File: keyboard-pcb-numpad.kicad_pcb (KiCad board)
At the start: 2 copper layers, 100 x 99 mm, 37 parts, among them SW1 SW_Push, U1 ProMicro

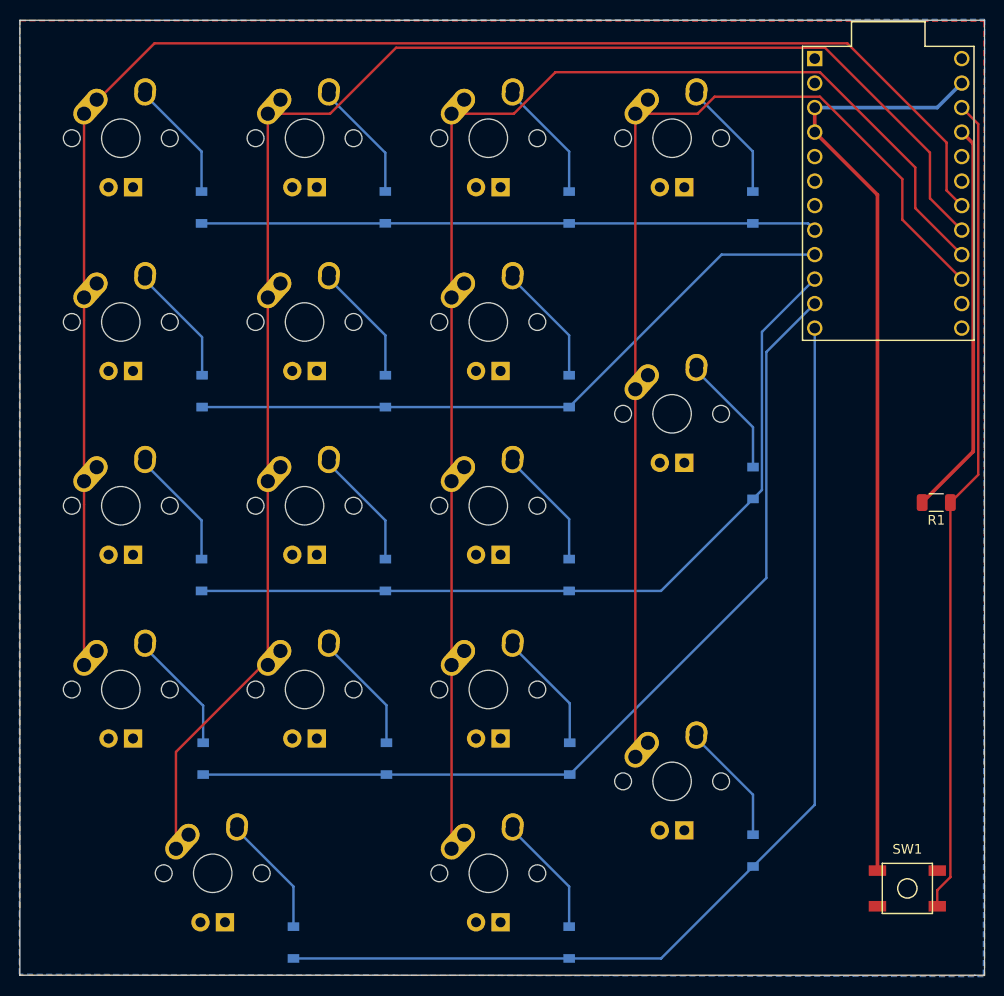
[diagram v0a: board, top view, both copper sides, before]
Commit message: fix: change switch footprints
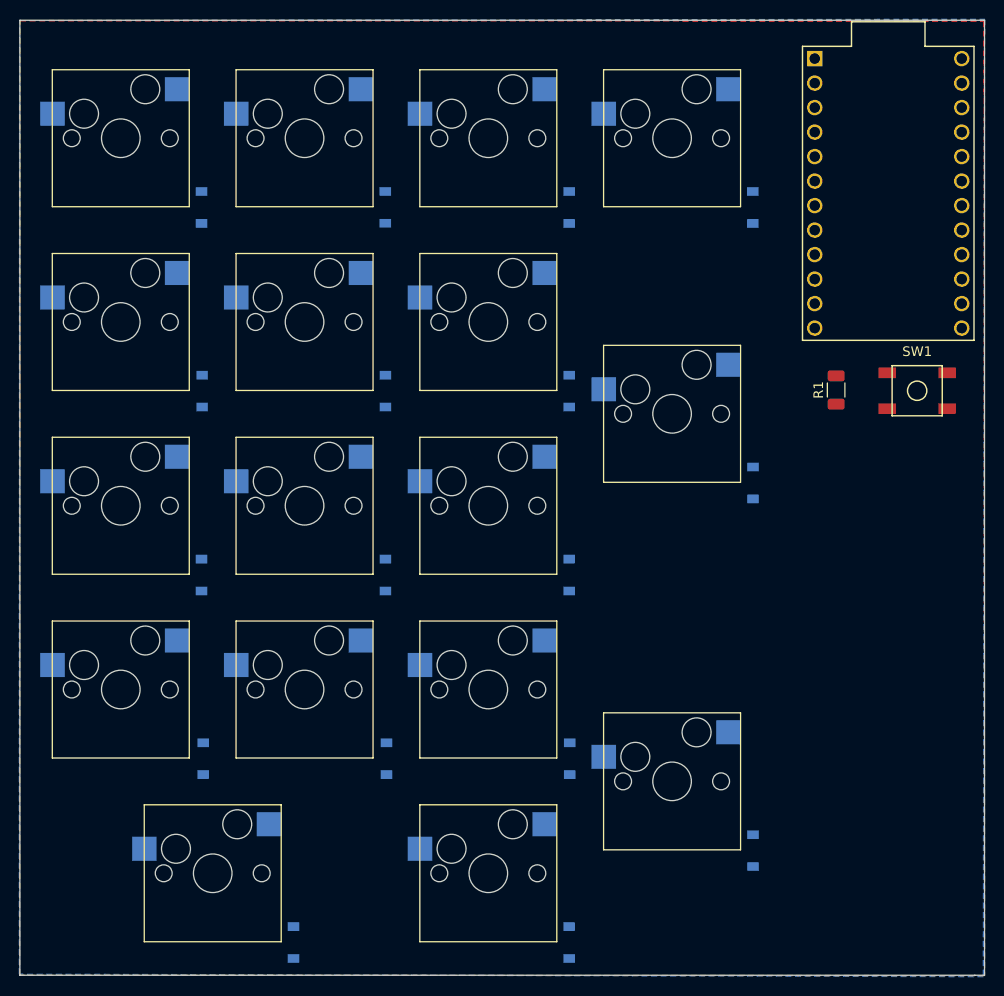
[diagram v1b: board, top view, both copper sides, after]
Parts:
- MX1, MX10, MX11, MX12, MX13, MX14, MX15, MX2, MX3, MX4, MX5, MX6, MX7, MX8: footprint MX_Alps_Hybrid:MX-1U -> Switch_Keyboard_Kailh:SW_Hotswap_Kailh_1.00u
- MX16, MX17: footprint MX_Alps_Hybrid:MX-1U -> Switch_Keyboard_Kailh:SW_Hotswap_Kailh_2.00u_Rotated
- MX9: footprint MX_Alps_Hybrid:MX-1U -> Switch_Keyboard_Kailh:SW_Hotswap_Kailh_2.00u
- moved SW1 51.6 mm to (131.0, 81.4)
- moved R1 15.6 mm to (122.6, 81.3), turned to 90 degrees
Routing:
- net COL1: track 165.8 -> 0.00 mm
- net COL0: track 161.0 -> 0.00 mm
- net COL2: track 141.2 -> 0.00 mm
- net COL3: track 111.5 -> 0.00 mm
- net ROW4: track 110.1 -> 0.00 mm
- net GND: track 98.1 -> 0.00 mm
- net ROW3: track 97.3 -> 0.00 mm
- net ROW2: track 86.6 -> 0.00 mm
- net /RST: track 85.3 -> 0.00 mm
- net ROW1: track 70.1 -> 0.00 mm
- net ROW0: track 63.9 -> 0.00 mm
- net +5V: track 41.1 -> 0.00 mm
- net Net-(D4-Pad2): track 12.5 -> 0.00 mm
- net Net-(D8-Pad2): track 12.5 -> 0.00 mm
- net Net-(D13-Pad2): track 12.5 -> 0.00 mm
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
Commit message: feat: update pcb
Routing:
- net COL2: track 0.00 -> 325.0 mm
- net COL3: track 0.00 -> 320.2 mm
- net COL1: track 0.00 -> 204.5 mm
- net COL0: track 0.00 -> 162.3 mm
- net ROW4: track 0.00 -> 110.3 mm
- net ROW3: track 0.00 -> 97.3 mm
- net ROW2: track 0.00 -> 86.6 mm
- net ROW1: track 0.00 -> 70.9 mm
- net ROW0: track 0.00 -> 63.9 mm
- net /RST: track 0.00 -> 45.2 mm
- net +5V: track 0.00 -> 30.7 mm
- net Net-(D4-Pad2): track 0.00 -> 11.7 mm
- net Net-(D8-Pad2): track 0.00 -> 11.7 mm
- net Net-(D13-Pad2): track 0.00 -> 11.7 mm
- net Net-(D2-Pad2): track 0.00 -> 11.7 mm
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
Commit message: fix: fix pcb
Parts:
- moved SW1 0.47 mm to (131.5, 81.5)
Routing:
- net GND: track 0.00 -> 44.6 mm
- net (no net): track 7.73 -> 0.00 mm
- net /RST: track 45.2 -> 49.4 mm
